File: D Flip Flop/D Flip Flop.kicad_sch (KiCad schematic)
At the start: 11 parts, among them J101 USB_A, SW101 SW_Push, SW102 SW_Push, SW103 SW_Push

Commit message: Completed first draft
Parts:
- added H101, H102, H103, H104: MountingHole, MountingHole:MountingHole_2.2mm_M2, symbol Mechanical:MountingHole
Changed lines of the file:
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@@
     (pin "2")
+  )
+  (symbol (lib_id "Mechanical:MountingHole") (at 226.06 121.92 0) (unit 1)
+    (in_bom yes) (on_board yes) (fields_autoplaced)
+    (property "Reference" "H102" (id 0) (at 228.6 120.6499 0)
+      (effects (font (size 1.27 1.27)) (justify left))
+    )
+    (property "Value" "MountingHole" (id 1) (at 228.6 123.1899 0)
+      (effects (font (size 1.27 1.27)) (justify left))
+    )
+    (property "Footprint" "MountingHole:MountingHole_2.2mm_M2" (id 2) (at 226.06 121.92 0)
+      (effects (font (size 1.27 1.27)) hide)
+    )
+    (property "Datasheet" "~" (id 3) (at 226.06 121.92 0)
+      (effects (font (size 1.27 1.27)) hide)
+    )
   )
   (symbol (lib_id "Device:LED") (at 222.25 69.215 90) (unit 1)
@@
     )
     (pin "1")
+  )
+  (symbol (lib_id "Mechanical:MountingHole") (at 226.06 129.54 0) (unit 1)
+    (in_bom yes) (on_board yes) (fields_autoplaced)
+    (property "Reference" "H103" (id 0) (at 228.6 128.2699 0)
+      (effects (font (size 1.27 1.27)) (justify left))
+    )
+    (property "Value" "MountingHole" (id 1) (at 228.6 130.8099 0)
+      (effects (font (size 1.27 1.27)) (justify left))
+    )
+    (property "Footprint" "MountingHole:MountingHole_2.2mm_M2" (id 2) (at 226.06 129.54 0)
+      (effects (font (size 1.27 1.27)) hide)
+    )
+    (property "Datasheet" "~" (id 3) (at 226.06 129.54 0)
+      (effects (font (size 1.27 1.27)) hide)
+    )
+  )
+  (symbol (lib_id "Mechanical:MountingHole") (at 226.06 137.795 0) (unit 1)
+    (in_bom yes) (on_board yes) (fields_autoplaced)
+    (property "Reference" "H104" (id 0) (at 228.6 136.5249 0)
+      (effects (font (size 1.27 1.27)) (justify left))
+    )
+    (property "Value" "MountingHole" (id 1) (at 228.6 139.0649 0)
+      (effects (font (size 1.27 1.27)) (justify left))
+    )
+    (property "Footprint" "MountingHole:MountingHole_2.2mm_M2" (id 2) (at 226.06 137.795 0)
+      (effects (font (size 1.27 1.27)) hide)
+    )
+    (property "Datasheet" "~" (id 3) (at 226.06 137.795 0)
+      (effects (font (size 1.27 1.27)) hide)
+    )
   )
   (symbol (lib_name "GND_1") (lib_id "power:GND") (at 222.25 77.47 0) (unit 1)
@@
     )
     (pin "1")
+  )
+  (symbol (lib_id "Mechanical:MountingHole") (at 226.06 113.665 0) (unit 1)
+    (in_bom yes) (on_board yes) (fields_autoplaced)
+    (property "Reference" "H101" (id 0) (at 228.6 112.3949 0)
+      (effects (font (size 1.27 1.27)) (justify left))
+    )
+    (property "Value" "MountingHole" (id 1) (at 228.6 114.9349 0)
+      (effects (font (size 1.27 1.27)) (justify left))
+    )
+    (property "Footprint" "MountingHole:MountingHole_2.2mm_M2" (id 2) (at 226.06 113.665 0)
+      (effects (font (size 1.27 1.27)) hide)
+    )
+    (property "Datasheet" "~" (id 3) (at 226.06 113.665 0)
+      (effects (font (size 1.27 1.27)) hide)
+    )
   )
   (symbol (lib_id "power:GND") (at 27.305 48.26 0) (unit 1)
@@
       (reference "D801") (unit 1) (value "LED") (footprint "LED_THT:LED_D3.0mm")
     )
+    (path "/9046592e-c911-4e5b-8525-9ab42fd9cbe9"
+      (reference "H101") (unit 1) (value "MountingHole") (footprint "MountingHole:MountingHole_2.2mm_M2")
+    )
+    (path "/167f0c5c-5e95-4178-8031-98c69e3bb919"
+      (reference "H102") (unit 1) (value "MountingHole") (footprint "MountingHole:MountingHole_2.2mm_M2")
+    )
+    (path "/1ea52a29-0c5b-418b-94e2-538aaa332c23"
+      (reference "H103") (unit 1) (value "MountingHole") (footprint "MountingHole:MountingHole_2.2mm_M2")
+    )
+    (path "/213326dd-57f1-4189-b051-da4fb33ad901"
+      (reference "H104") (unit 1) (value "MountingHole") (footprint "MountingHole:MountingHole_2.2mm_M2")
+    )
     (path "/d8f67db2-7a59-475e-9e92-ae4e73d75ca6"

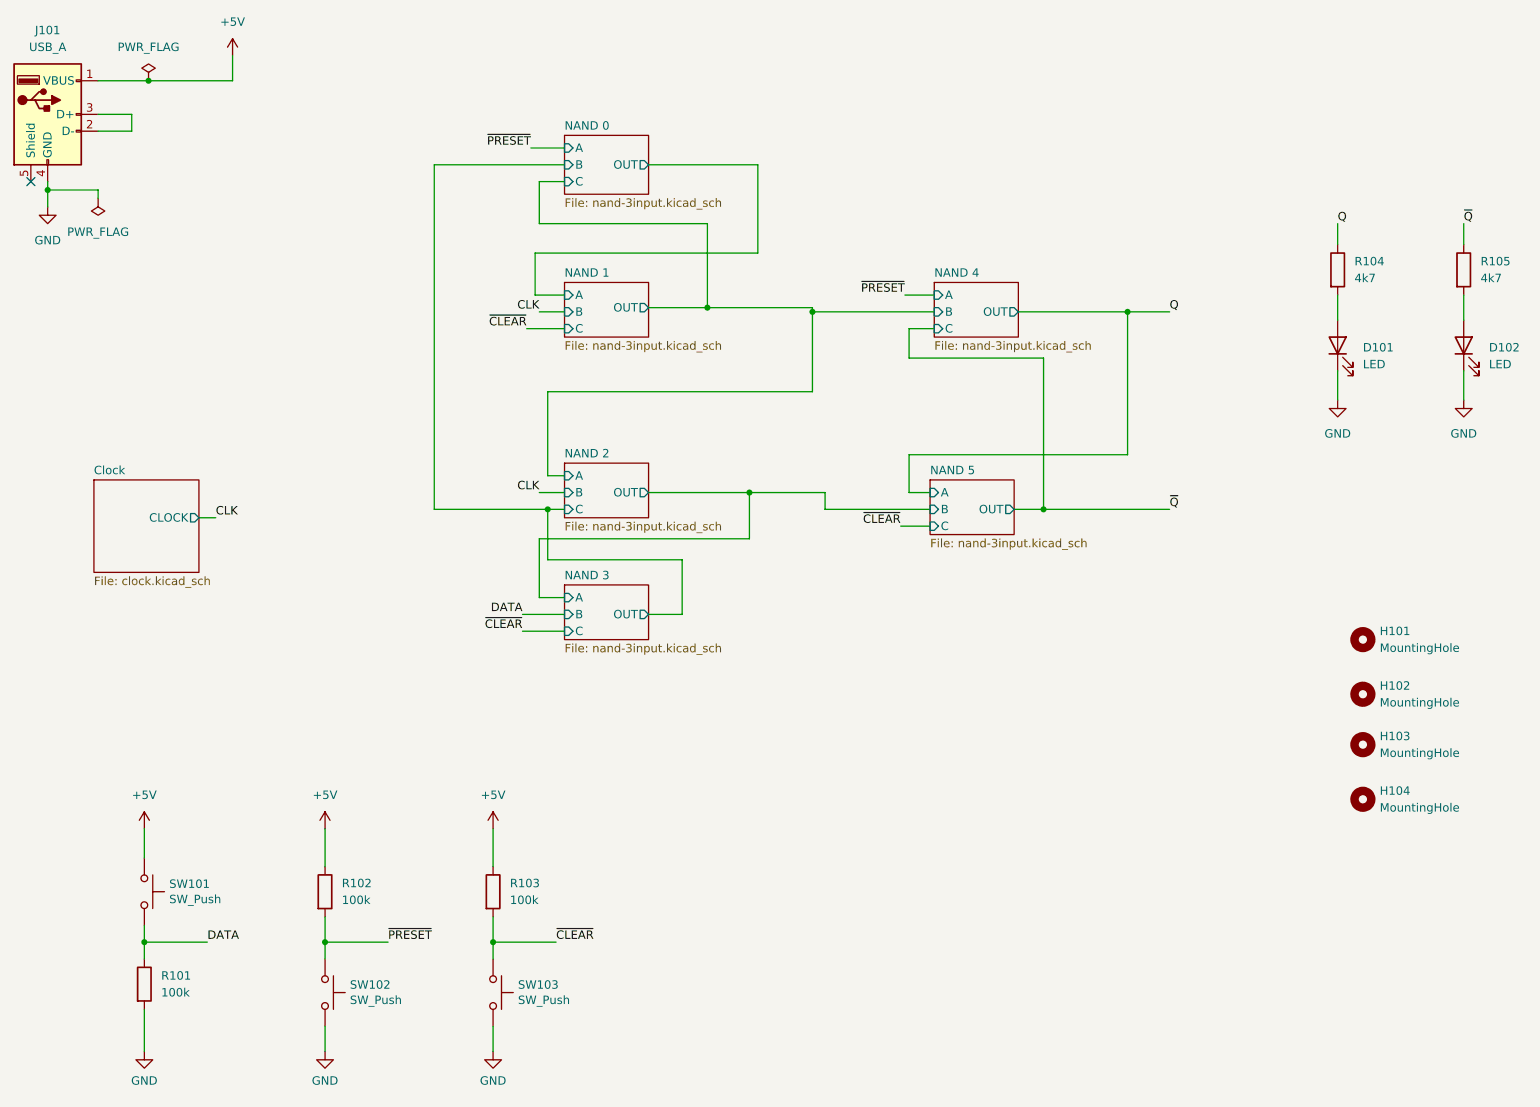
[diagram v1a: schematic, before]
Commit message: Don't need monostable for clock
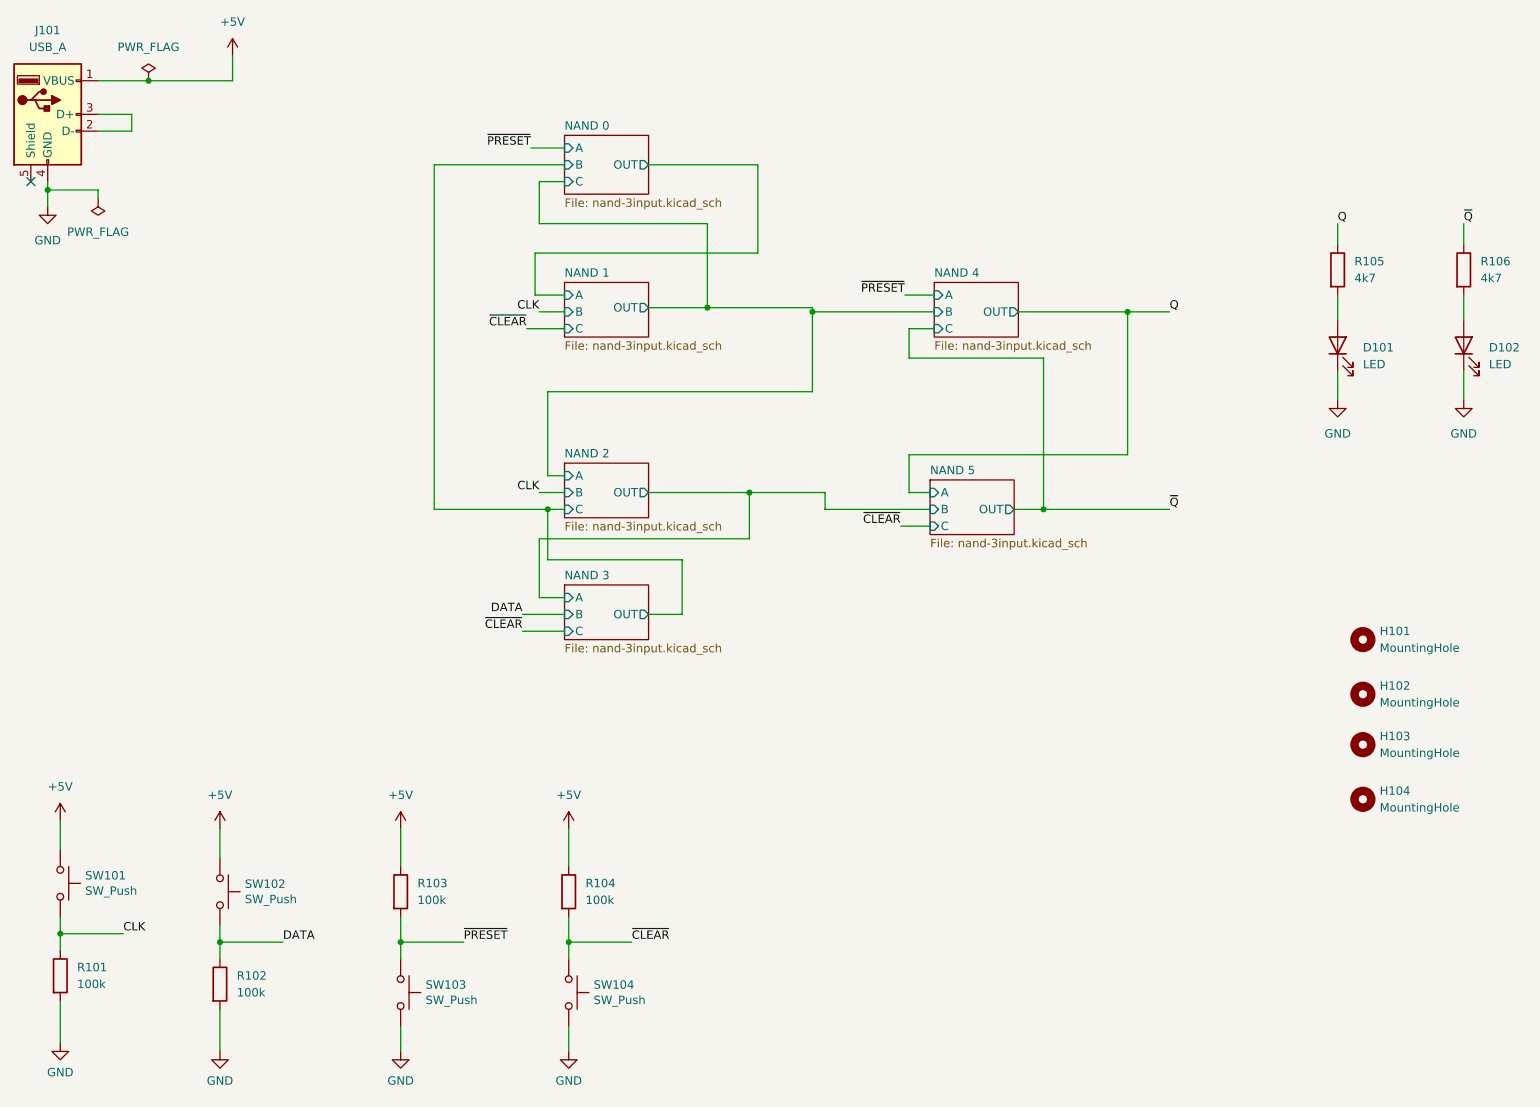
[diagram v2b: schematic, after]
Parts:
- added R101: 100k, Resistor_THT:R_Axial_DIN0207_L6.3mm_D2.5mm_P7.62mm_Horizontal, symbol Device:R
- added SW101: SW_Push, Button_Switch_THT:SW_PUSH_6mm_H4.3mm, symbol Switch:SW_Push
- renumbered R101 to R102, R102 to R103, R103 to R104, R104 to R105, R105 to R106, SW101 to SW102, SW102 to SW103, SW103 to SW104
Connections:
- net +5V: now also SW101.1
- net CLK: now also R101.1, SW101.2
- net GND: now also R101.2
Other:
- removed sheet Clock
- moved on the sheet: R102, R103, R104, SW102, SW103, SW104

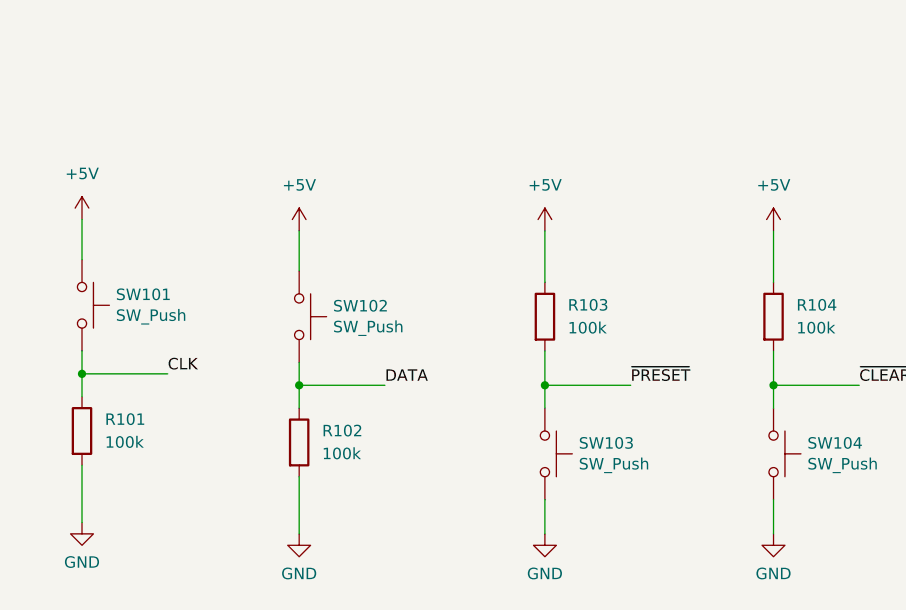
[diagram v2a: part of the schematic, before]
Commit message: Simplifying board a little
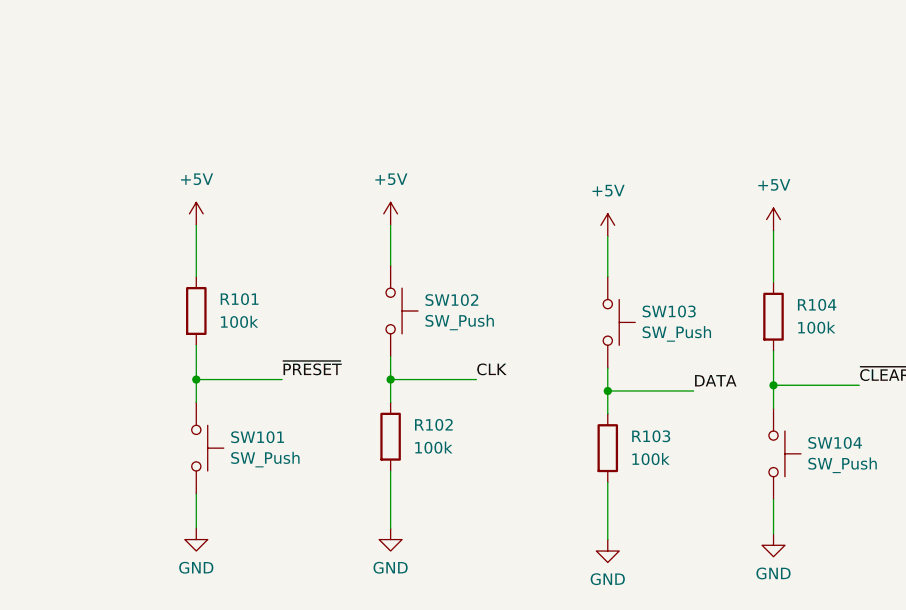
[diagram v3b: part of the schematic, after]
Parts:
- renumbered R103 to R101, R101 to R102, R102 to R103, SW103 to SW101, SW101 to SW102, SW102 to SW103
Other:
- moved on the sheet: R101, R102, R103, SW101, SW102, SW103
